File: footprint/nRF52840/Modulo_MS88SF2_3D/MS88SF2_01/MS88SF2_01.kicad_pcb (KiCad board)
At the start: 2 copper layers, 17.4 x 23.2 mm, 1 part, among them U1 MS88SF2-castellate

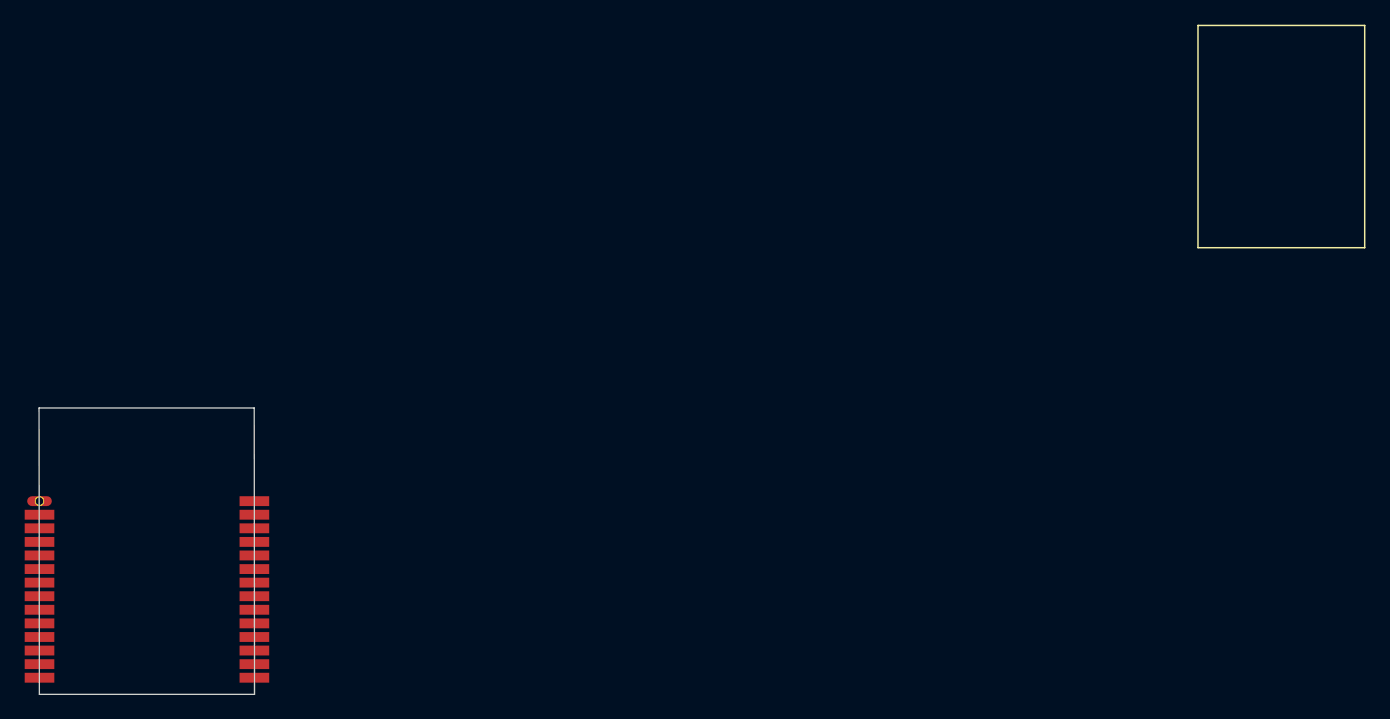
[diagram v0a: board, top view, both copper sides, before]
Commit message: Add MS88SF2
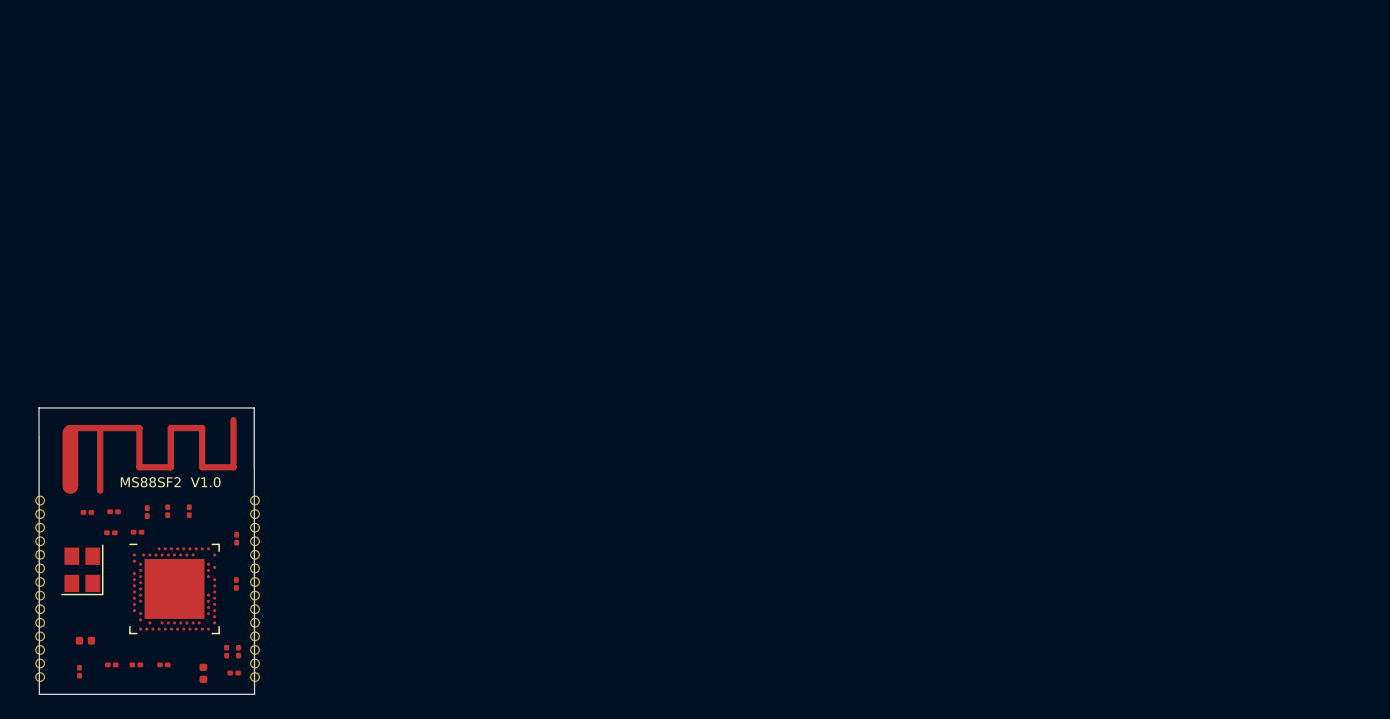
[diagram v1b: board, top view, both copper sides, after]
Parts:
- added REF**: C_0201_0603Metric, Capacitor_SMD:C_0201_0603Metric, F.Cu at (141.0, 111.3)
- added REF**: C_0201_0603Metric, Capacitor_SMD:C_0201_0603Metric, F.Cu at (137.0, 98.9)
- added REF**: C_0201_0603Metric, Capacitor_SMD:C_0201_0603Metric, F.Cu at (138.9, 100.5)
- added REF**: C_0201_0603Metric, Capacitor_SMD:C_0201_0603Metric, F.Cu at (146.1, 110.2)
- added REF**: C_0201_0603Metric, Capacitor_SMD:C_0201_0603Metric, F.Cu at (139.7, 98.9)
- added REF**: C_0201_0603Metric, Capacitor_SMD:C_0201_0603Metric, F.Cu at (141.4, 98.8)
- added REF**: C_0402_1005Metric, Capacitor_SMD:C_0402_1005Metric, F.Cu at (134.7, 109.3)
- added REF**: C_0201_0603Metric, Capacitor_SMD:C_0201_0603Metric, F.Cu at (136.8, 100.6)
- added REF**: C_0201_0603Metric, Capacitor_SMD:C_0201_0603Metric, F.Cu at (134.8, 98.9)
- added REF**: C_0402_1005Metric, Capacitor_SMD:C_0402_1005Metric, F.Cu at (144.2, 111.9)
- added REF**: Crystal_SMD_TXC_7M-4Pin_3.2x2.5mm, Crystal:Crystal_SMD_TXC_7M-4Pin_3.2x2.5mm, F.Cu at (134.4, 103.6)
- added REF**: C_0201_0603Metric, Capacitor_SMD:C_0201_0603Metric, F.Cu at (146.7, 111.9)
- added REF**: Nordic_AQFN-73-1EP_7x7mm_P0.5mm, Package_DFN_QFN:Nordic_AQFN-73-1EP_7x7mm_P0.5mm, F.Cu at (141.9, 105.1)
- added REF**: C_0201_0603Metric, Capacitor_SMD:C_0201_0603Metric, F.Cu at (138.8, 111.3)
- added REF**: C_0201_0603Metric, Capacitor_SMD:C_0201_0603Metric, F.Cu at (143.1, 98.8)
- added REF**: C_0201_0603Metric, Capacitor_SMD:C_0201_0603Metric, F.Cu at (146.9, 101.0)
- added REF**: C_0201_0603Metric, Capacitor_SMD:C_0201_0603Metric, F.Cu at (136.8, 111.3)
- added REF**: C_0201_0603Metric, Capacitor_SMD:C_0201_0603Metric, F.Cu at (146.9, 104.7)
- added REF**: C_0201_0603Metric, Capacitor_SMD:C_0201_0603Metric, F.Cu at (134.2, 111.8)
- added REF**: C_0201_0603Metric, Capacitor_SMD:C_0201_0603Metric, F.Cu at (147.1, 110.2)
- moved U1 0.07 mm to (139.7, 104.9)
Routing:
- net (no net): track 0.00 -> 36.1 mm
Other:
- board text added: "MS88SF2 V1.0"

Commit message: update
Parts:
- removed U1: MS88SF2-castellate, MS88SF2_01:MS88SF2-castellate
- added REF**: MS88SF2_v2, MS88SF2_01:MS88SF2_v2, B.Cu at (147.5, 98.7)
- added REF**: MS88SF2_v2, MS88SF2_01:MS88SF2_v2, F.Cu at (131.7, 98.7)
- moved REF** 1.41 mm to (140.5, 105.4)
- moved REF** 1.24 mm to (145.7, 101.0)
- moved REF** 1.22 mm to (145.7, 104.7)
- moved REF** 0.91 mm to (145.8, 111.9)
- moved REF** 0.91 mm to (146.2, 110.2)
- moved REF** 0.91 mm to (145.2, 110.2)
- moved REF** 0.91 mm to (143.3, 111.9)
